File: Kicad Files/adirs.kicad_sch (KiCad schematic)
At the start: 8 parts, among them SW24 GND_CTL, SW25 ADR_1, SW26 ADR_2, SW27 ADR_3

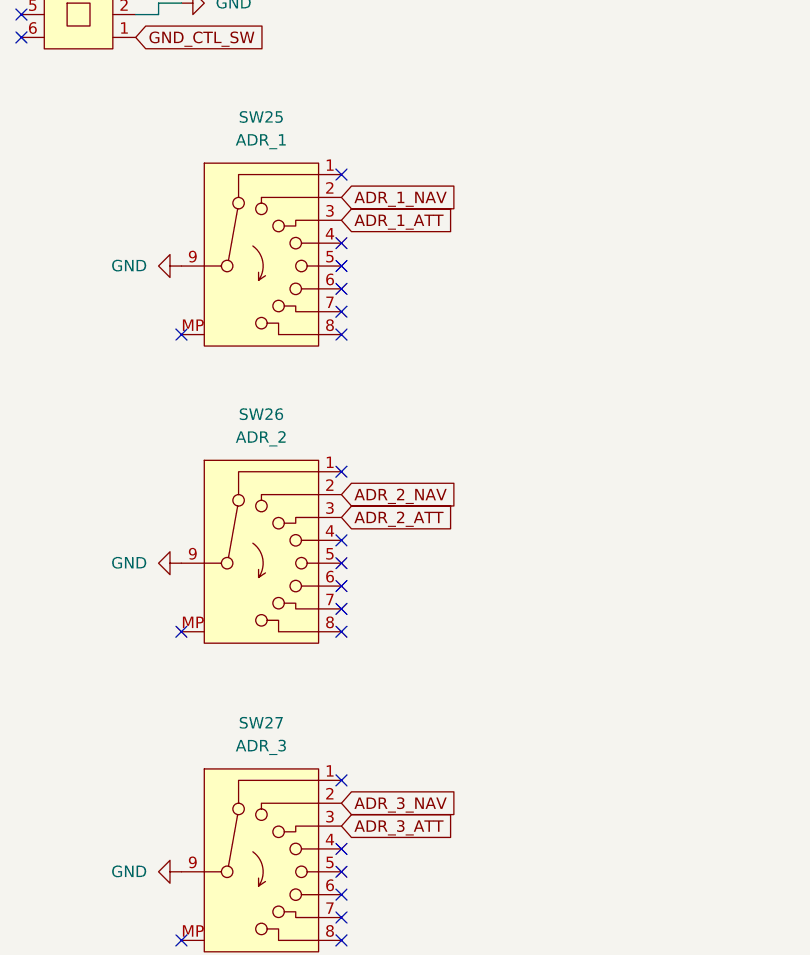
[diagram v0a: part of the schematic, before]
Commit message: VsCode firmware file + changes in the PCB layout
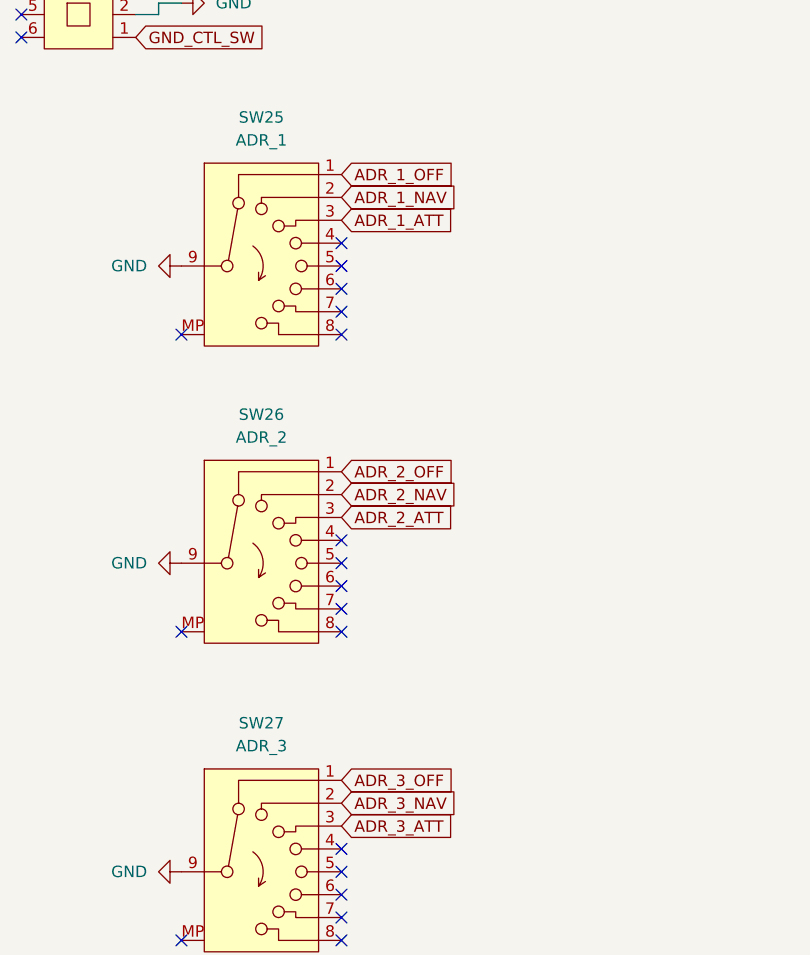
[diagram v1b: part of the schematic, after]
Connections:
- net ADR_3_OFF: now reaches SW27.1
- net ADR_2_OFF: now reaches SW26.1
- net ADR_1_OFF: now reaches SW25.1
- no-connect marks 25 -> 22
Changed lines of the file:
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@@
-	)
-	(no_connect
-		(at 55.88 44.45)
 	)
 	(no_connect
@@
 	(no_connect
 		(at 55.88 129.54)
-	)
-	(no_connect
-		(at 55.88 111.76)
-	)
-	(no_connect
-		(at 55.88 77.47)
 	)
 	(no_connect
@@
 		)
 	)
+	(global_label "ADR_1_OFF"
+		(shape input)
+		(at 55.88 44.45 0)
+		(fields_autoplaced yes)
+		(effects
+			(font
+				(size 1.27 1.27)
+			)
+			(justify left)
+		)
+		(property "Intersheetrefs" "${INTERSHEET_REFS}"
+			(at 69.1462 44.45 0)
+			(effects
+				(font
+					(size 1.27 1.27)
+				)
+				(justify left)
+				(hide yes)
+			)
+		)
+	)
 	(global_label "GND_CTL_SW"
 		(shape input)
@@
 			(effects
 				(font
+					(size 1.27 1.27)
+				)
+				(justify left)
+				(hide yes)
+			)
+		)
+	)
+	(global_label "ADR_3_OFF"
+		(shape input)
+		(at 55.88 111.76 0)
+		(fields_autoplaced yes)
+		(effects
+			(font
+				(size 1.27 1.27)
+			)
+			(justify left)
+		)
+		(property "Intersheetrefs" "${INTERSHEET_REFS}"
+			(at 69.1462 111.76 0)
+			(effects
+				(font
+					(size 1.27 1.27)
+				)
+				(justify left)
+				(hide yes)
+			)
+		)
+	)
+	(global_label "ADR_2_OFF"
+		(shape input)
+		(at 55.88 77.47 0)
+		(fields_autoplaced yes)
+		(effects
+			(font
+				(size 1.27 1.27)
+			)
+			(justify left)
+		)
+		(property "Intersheetrefs" "${INTERSHEET_REFS}"
+			(at 69.1462 77.47 0)
+			(effects
+				(font

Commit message: New STL files for APU OVHD element, other coming in the next few weeks
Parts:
- SW24: footprint SFLibrary:G-Switch PS-7054DVB-6PN -> PCM_SFLibrary:G-Switch PS-7054DVB-6PN
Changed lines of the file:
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@@
 (kicad_sch
-	(version 20231120)
+	(version 20250114)
 	(generator "eeschema")
-	(generator_version "8.0")
+	(generator_version "9.0")
 	(paper "A4")
 	(no_connect
@@
 			)
 		)
-		(property "Footprint" "SFLibrary:G-Switch PS-7054DVB-6PN"
+		(property "Footprint" "PCM_SFLibrary:G-Switch PS-7054DVB-6PN"
 			(at 27.94 33.02 0)
 			(effects
